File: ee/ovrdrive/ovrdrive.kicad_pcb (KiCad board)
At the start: 4 copper layers, 36.6 x 15 mm, 43 parts, among them J1 USB_A, J3 AVR-ISP-6, U1 SM3257ENT, U2 FLASH, U3 ATtiny24A-MM, U4 SN74LVC1G32DCKR, U5 DRV8837C

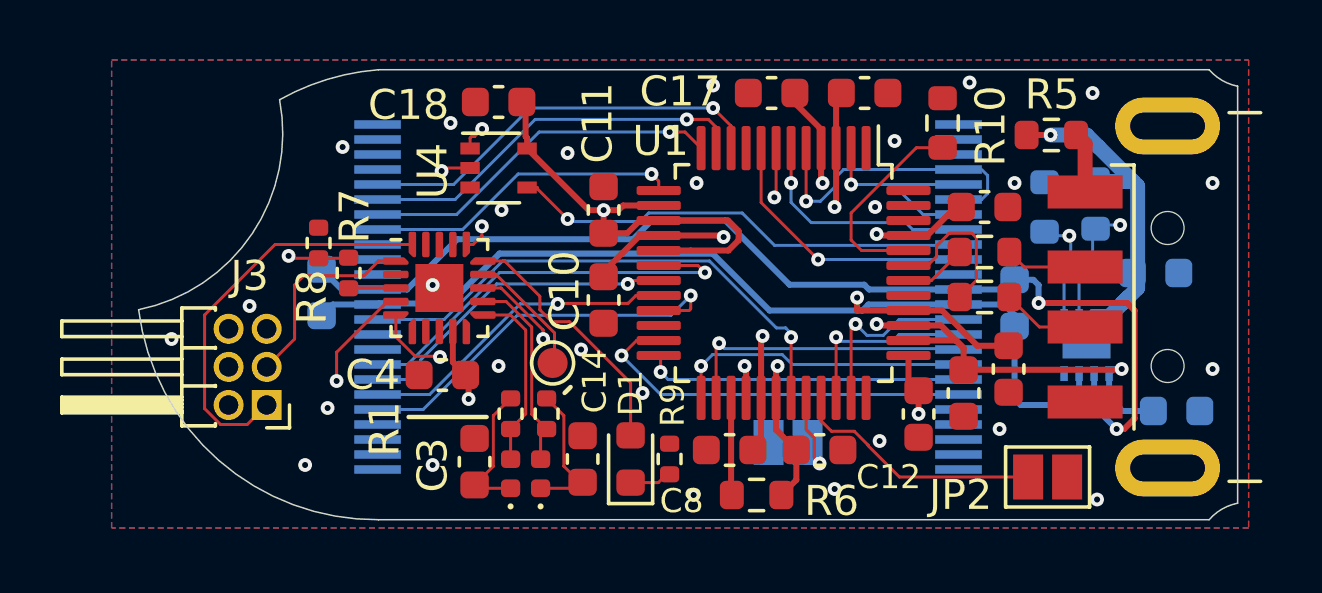
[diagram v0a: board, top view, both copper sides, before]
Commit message: Released R0.4 for *quote only*. Still need to do a final revision before sending off.
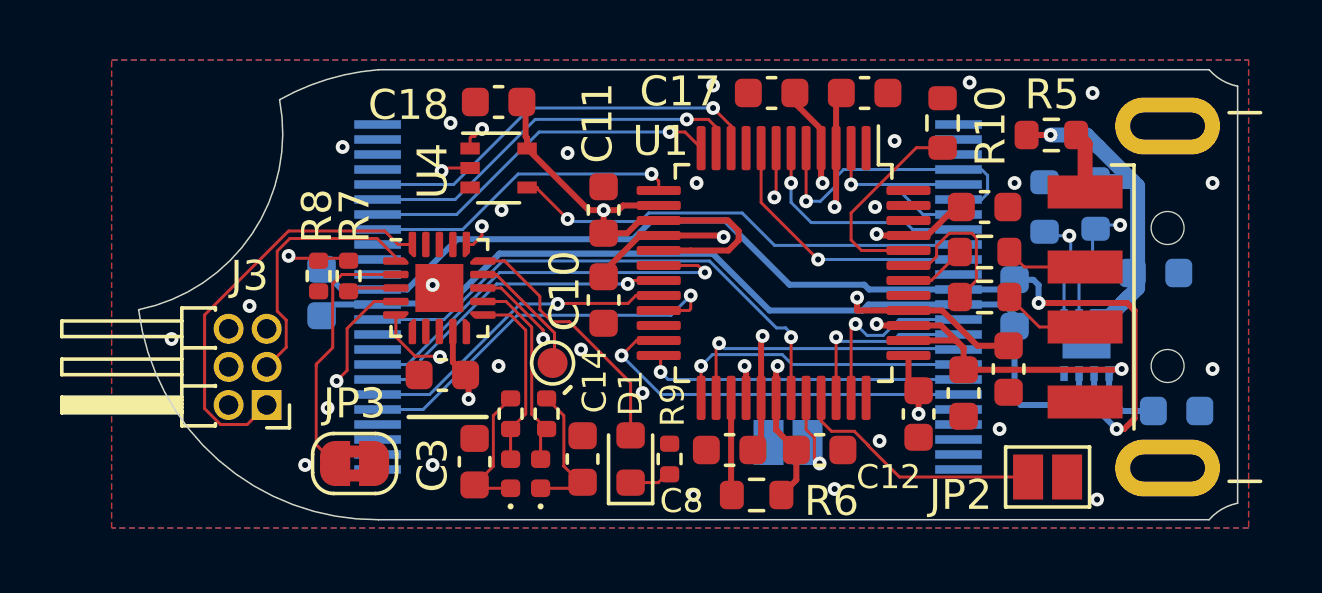
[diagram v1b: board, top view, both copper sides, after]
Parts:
- added JP3: SolderJumper_2_Bridged, Jumper:SolderJumper-2_P1.3mm_Bridged2Bar_RoundedPad1.0x1.5mm, F.Cu at (115.0, 109.8)
- moved R8 1.10 mm to (113.8, 103.5), turned to 90 degrees
- moved R7 0.10 mm to (114.8, 103.5)
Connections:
- U3 pad 2: unconnected-(U3-PA3-Pad2) -> Net-(JP3-B)
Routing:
- net Net-(JP3-B): track 0.00 -> 8.71 mm
- net /SCK: track 6.82 -> 8.77 mm
